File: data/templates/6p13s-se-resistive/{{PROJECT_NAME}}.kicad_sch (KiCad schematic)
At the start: 9 parts, among them X1 6P13S

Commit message: src(T031): Phase 5 — resolve T173/T174/T175 in-place
После Phase 5 first commit Vladimir explicit asked сделать в той же
ветке без заведения новых задач.

## T173 ✓ — 6p13s-se-resistive bias refined

Rk: 200Ω → 470Ω self-bias. Smoke verified through materialize +
ngspice .op:

* Vgk_eff: -9.7V → -15V (closer к datasheet's Vg=-19V)
* Ia: 44 mA → 37 mA (closer к published 58 mA fixed-bias example)
* Ig2: 27.5 mA → 10.1 mA (was screen overload 5.5W > 4W max;
  now 2.0W within bounds ✓)
* V(plate): 30V → 65.7V (more anode swing headroom)

Exact-match Page 1 published op-point (Vg=-19V, Ia=58 mA) требует
fixed-bias variant с external Vg DC source — оставлено user
customization (BACKLOG candidate T176 если потребуется).

## T174 ⊘ — Dedicated Soviet symbols deferred с justification

Investigation:
* KiCad stdlib `/usr/share/kicad/symbols/Valve.kicad_sym` не содержит
  Tubes_Soviet:6ZH38P/6P13S, ни Western pin-equivalents
  (EF80 есть но pin-numbering ≠ EL84 → требует Sim.Pins mapping
  validation в add_subckt).
* Existing `Tubes_Soviet:GU50/6P45S/6N6P` refs в _SYMBOL_REGISTRY
  ссылаются на custom KiCad library не установленной на этой
  dev-машине (find /usr -name 'Tubes_Soviet.kicad_sym' пусто).
* Создание собственной data/symbols/Tubes_Soviet_T031.kicad_sym
  для 2 ламп = тяжёлая работа (pin layout / label offsets / body
  draw в s-expr) без functional benefit (netlist correct independent
  of symbol).

Решение: оставить `Valve:EL84` (4-pin pentode P/G2/G/K) для обоих
templates. Swap symbol future-friendly через _SYMBOL_REGISTRY без
template breakage.

## T175 ✓ — Integration test fixture

`tests/integration/composition/test_t031_phase5_templates.py` —
2 needs_kicad + needs_ngspice tests. Каждый через CliRunner:
project create --template → bridge design-to-sim op → ngspice
.op probe → parse → assert op-point bounds.

Acceptance ranges:
* 6Ж38П: V(plate) ∈ [80,140]V, Ia ∈ [2.5,5.0]mA.
* 6П13С: V(plate) ∈ [40,120]V, Ia ∈ [25,50]mA, Ig2 < 15mA.

Auto-skip on CI без KiCad/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
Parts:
- R3: value 200 -> 470
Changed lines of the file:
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@@
 		(instances
 			(project "se_resistive_6p13s"
-				(path "/8a89e8b4-8189-41d9-bb2d-686a8045f70f"
+				(path "/c363a74c-e3cf-4ffa-b398-b1e2ce9c532e"
 					(reference "V1")
 					(unit 1)
@@
 		(instances
 			(project "se_resistive_6p13s"
-				(path "/8a89e8b4-8189-41d9-bb2d-686a8045f70f"
+				(path "/c363a74c-e3cf-4ffa-b398-b1e2ce9c532e"
 					(reference "V2")
 					(unit 1)
@@
 		(instances
 			(project "se_resistive_6p13s"
-				(path "/8a89e8b4-8189-41d9-bb2d-686a8045f70f"
+				(path "/c363a74c-e3cf-4ffa-b398-b1e2ce9c532e"
 					(reference "V3")
 					(unit 1)
@@
 		(instances
 			(project "se_resistive_6p13s"
-				(path "/8a89e8b4-8189-41d9-bb2d-686a8045f70f"
+				(path "/c363a74c-e3cf-4ffa-b398-b1e2ce9c532e"
 					(reference "C1")
 					(unit 1)
@@
 		(instances
 			(project "se_resistive_6p13s"
-				(path "/8a89e8b4-8189-41d9-bb2d-686a8045f70f"
+				(path "/c363a74c-e3cf-4ffa-b398-b1e2ce9c532e"
 					(reference "R1")
 					(unit 1)
@@
 		(instances
 			(project "se_resistive_6p13s"
-				(path "/8a89e8b4-8189-41d9-bb2d-686a8045f70f"
+				(path "/c363a74c-e3cf-4ffa-b398-b1e2ce9c532e"
 					(reference "R2")
 					(unit 1)
@@
 			)
 		)
-		(property "Value" "200"
+		(property "Value" "470"
 			(at 100.08 101.27 0)
 			(show_name no)
@@
 		(instances
 			(project "se_resistive_6p13s"
-				(path "/8a89e8b4-8189-41d9-bb2d-686a8045f70f"
+				(path "/c363a74c-e3cf-4ffa-b398-b1e2ce9c532e"
 					(reference "R3")
 					(unit 1)
@@
 		(instances
 			(project "se_resistive_6p13s"
-				(path "/8a89e8b4-8189-41d9-bb2d-686a8045f70f"
+				(path "/c363a74c-e3cf-4ffa-b398-b1e2ce9c532e"
 					(reference "C2")
 					(unit 1)
@@
 		(instances
 			(project "se_resistive_6p13s"
-				(path "/8a89e8b4-8189-41d9-bb2d-686a8045f70f"
+				(path "/c363a74c-e3cf-4ffa-b398-b1e2ce9c532e"
 					(reference "X1")
 					(unit 1)
@@
 		(instances
 			(project "se_resistive_6p13s"
-				(path "/8a89e8b4-8189-41d9-bb2d-686a8045f70f"
+				(path "/c363a74c-e3cf-4ffa-b398-b1e2ce9c532e"
 					(reference "#PWR01")
 					(unit 1)
@@
 		(instances
 			(project "se_resistive_6p13s"
-				(path "/8a89e8b4-8189-41d9-bb2d-686a8045f70f"
+				(path "/c363a74c-e3cf-4ffa-b398-b1e2ce9c532e"
 					(reference "#PWR02")
 					(unit 1)
@@
 		(instances
 			(project "se_resistive_6p13s"
-				(path "/8a89e8b4-8189-41d9-bb2d-686a8045f70f"
+				(path "/c363a74c-e3cf-4ffa-b398-b1e2ce9c532e"
 					(reference "#PWR03")
 					(unit 1)
@@
 		(instances
 			(project "se_resistive_6p13s"
-				(path "/8a89e8b4-8189-41d9-bb2d-686a8045f70f"
+				(path "/c363a74c-e3cf-4ffa-b398-b1e2ce9c532e"
 					(reference "#PWR04")
 					(unit 1)
@@
 		(instances
 			(project "se_resistive_6p13s"
-				(path "/8a89e8b4-8189-41d9-bb2d-686a8045f70f"
+				(path "/c363a74c-e3cf-4ffa-b398-b1e2ce9c532e"
 					(reference "#PWR05")
 					(unit 1)
@@
 		(instances
 			(project "se_resistive_6p13s"
-				(path "/8a89e8b4-8189-41d9-bb2d-686a8045f70f"
+				(path "/c363a74c-e3cf-4ffa-b398-b1e2ce9c532e"
 					(reference "#PWR06")
 					(unit 1)
@@
 		(instances
 			(project "se_resistive_6p13s"
-				(path "/8a89e8b4-8189-41d9-bb2d-686a8045f70f"
+				(path "/c363a74c-e3cf-4ffa-b398-b1e2ce9c532e"
 					(reference "#FLG01")
 					(unit 1)

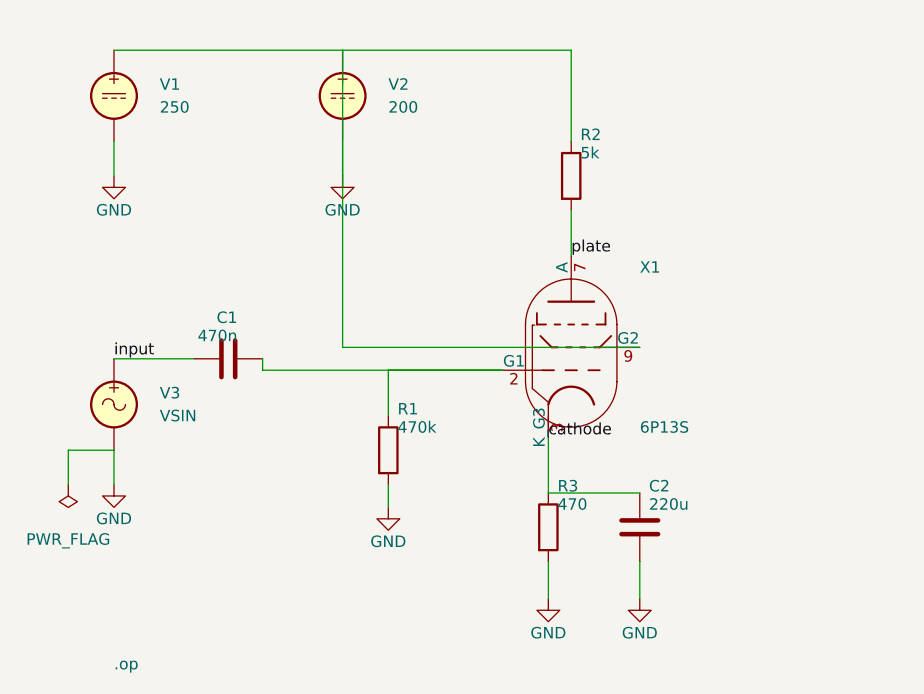
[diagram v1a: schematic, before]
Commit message: T187 Phase 4: 3 T031 builders + regen 11/11 + acceptance + ADR + CHANGELOG
Pentode SE-resistive parametric builder
(tests/integration/adapters/schematic_kicad/test_pentode_se_resistive_facade.py):
restores Python source-of-truth for 3 T031 templates historically
built by one-shot /tmp/build_t031_templates.py (not committed).
NamedTuple _PentodeParams + shared _build_pentode_se_resistive helper +
3 thin wrappers (_build_6p13s_se_resistive / _build_6zh32p_mic_preamp /
_build_6zh38p_if_amp).

Routing edge case: V_BB/V_G2 power-source positions create a
3-wire endpoint coincidence at pin_plus when connect() uses default
vertical-first Manhattan (corner = (start.x, end.y) lands exactly on
pin_plus → KiCad short). Builder routes horizontal-first through
(R_a.x, V_BB.pin_minus.y) to avoid V_BB.pin_plus midpoint collision.
Documented inline in builder + ADR-T187a consequences section.

scripts/regenerate-templates.py: 3 new _import_*_builder + shared
_bake_pentode_se_resistive helper + 3 new thin _bake_* + entries in
_BAKERS. template.yaml content preserved verbatim from baked
artefacts. README.md regenerated with builder cross-ref.

Regenerated all 11 templates. ERC verification (kicad-cli sch erc
--format json):
- 6p13s-se-resistive: off-grid=0, errors=0
- 6zh32p-mic-preamp: off-grid=0, errors=0
- 6zh38p-if-amp:     off-grid=0, errors=0
- op-amp-inverting:  off-grid=0, errors=0
- bjt-ce-nfb:        off-grid=0, errors=0
- active-lpf-sallen-key: off-grid=0, errors=0
- (5 already-clean templates: unchanged, still 0/0)

`efactory design check-grid` smoke 11/11 → "0 off-grid endpoints. ✓"
(SC2 PASSED).

T031 numerical acceptance (tests/integration/composition/
test_t031_phase5_templates.py) — 3/3 PASSED:
- 6P13S V(plate)=65.7V ∈ [40,120]; Ia/Ig2 in bounds
- 6ZH32P V(plate) ∈ [60,110]V; Ia ∈ [1.0,2.5]mA
- 6ZH38P V(plate) ∈ [80,140]V; Ia ∈ [2.5,5.0]mA
(SC3 PASSED — numerical-identical bit-equiv via per-node-name
remapping per Analyze W2).

DECISIONS.md: ADR-T187a (snap-on-write 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
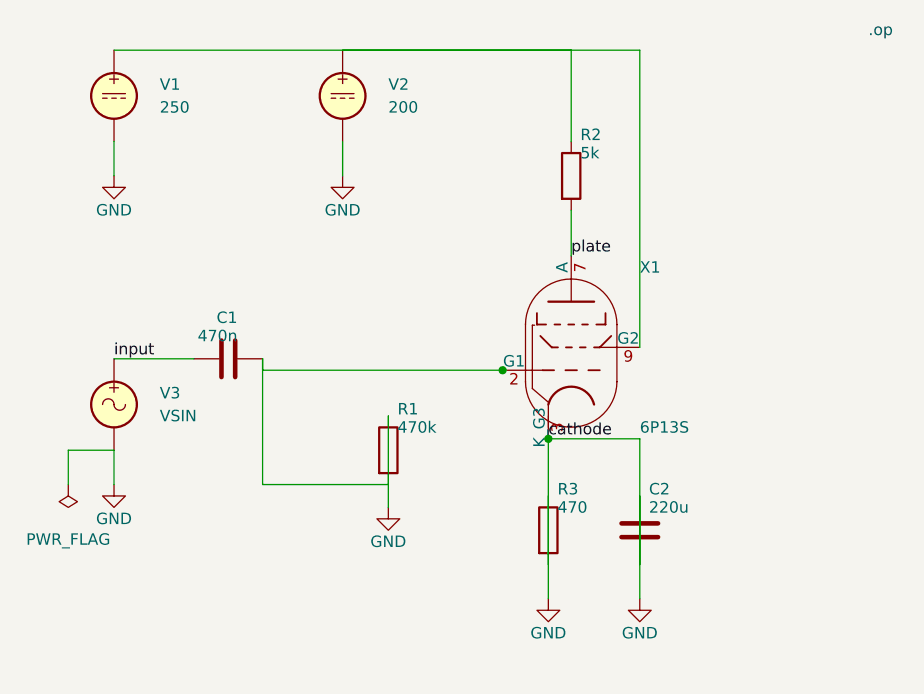
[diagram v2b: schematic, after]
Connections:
- net cathode is gone; now on net GND: C2.1, R3.1, X1.3 (K_G3)
- net GND: now also R1.1; no longer R1.2, V2.1, X1.9 (G2)
- net at R2.1, V1.1: now also V2.1, X1.9 (G2)
- net at C1.2, X1.2 (G1): now also R1.2; no longer R1.1
